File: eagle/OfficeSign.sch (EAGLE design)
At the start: 68 parts, among them Q1 16MHZ, SW3 KMR2, SW4 KMR2, U1 ATMEGA328, U2 L7805CDT-TR, U3 NCS36000, U4 PIR, U5 WS2801, U6 SPX3819, U8 TXB0108PWR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

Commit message: Move Files Around
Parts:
- removed U$10: FIDUCIAL, adafruit:FIDUCIAL
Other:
- moved on the sheet: C16, C17, U8

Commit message: WIP
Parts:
- removed D11: MBR120, microbuilder:DIODE-SCHOTTKYSOD-123
- added D2: MBR120, microbuilder:DIODE-SCHOTTKYSOD-123
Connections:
- net STROBE renamed D2
- removed net D5: U1.PD5(T1)
- removed net D6: U1.PD6(AIN0)
- removed net GPIO4: X2.GPIO5
- removed net GPIO5: X2.GPIO4
- removed net N$17: C15.1, D10.C, D11.C, R21.1, U6.IN
- removed net RST7: U1.PD3(INT1)
- removed net VBAT: D11.A
- new net N$23: C15.1, D10.C, D2.C, R21.1, U6.IN
- new net OCC: U1.PD5(T1), U8.B5
- new net OCC_ESP: U8.A5, X2.GPIO5
- new net RES: U1.PD6(AIN0), U8.B6
- new net RES_ESP: U8.A6, X2.GPIO4
- net OUT: now also U1.PD3(INT1)
- net VCC: now also D2.A
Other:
- moved on the sheet: C14, C15, C16, C17, D10, D12, D8, D9, JP6, R18, R19, R20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

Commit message: Moves and Shakes
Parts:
- added POT: (no value), SparkFun-Connectors:M04JST-PTH
- added R15: 3.3, adafruit:R-US_M0805
- added U7: NJVMJD2955T4G, bg_eagle_lib:NJVMJD2955T4G
- C19: value 10uF -> 0.33uF
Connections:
- new net N$24: POT.3
- new net N$25: POT.2
- new net N$26: JP4.PWR, R15.2, U7.E
- net GND: now also POT.1
- net RAW: now also R15.1, U7.B; no longer JP4.PWR
- net VCC: now also POT.4, U7.C
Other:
- moved on the sheet: C10, C19, JP4, LED1, R11, U2

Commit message: Add Indicator
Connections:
- removed net A1: U1.PC1(ADC1)
- removed net N$24: POT.3
- new net POT: POT.3, U1.PC1(ADC1)
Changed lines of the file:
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@@
 <?xml version="1.0" encoding="utf-8"?>
 <!DOCTYPE eagle SYSTEM "eagle.dtd">
-<eagle version="8.7.0">
+<eagle version="8.7.1">
 <drawing>
 <settings>
@@
 </segment>
 </net>
-<net name="A1" class="0">
+<net name="POT" class="0">
 <segment>
 <wire x1="231.14" y1="160.02" x2="233.68" y2="160.02" width="0.1524" layer="91"/>
 <pinref part="U1" gate="G$1" pin="PC1(ADC1)"/>
 <label x="233.68" y="160.02" size="1.27" layer="95" xref="yes"/>
+</segment>
+<segment>
+<pinref part="POT" gate="G$1" pin="3"/>
+<wire x1="25.4" y1="254" x2="27.94" y2="254" width="0.1524" layer="91"/>
+<label x="27.94" y="254" size="1.27" layer="95" xref="yes"/>
 </segment>
 </net>
@@
 </segment>
 </net>
-<net name="N$24" class="0">
-<segment>
-<pinref part="POT" gate="G$1" pin="3"/>
-<wire x1="25.4" y1="254" x2="27.94" y2="254" width="0.1524" layer="91"/>
-</segment>
-</net>

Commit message: wip
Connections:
- net D2 renamed POD_IND
- net N$25 renamed POT_IND
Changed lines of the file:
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@@
 </segment>
 </net>
-<net name="D2" class="0">
+<net name="POD_IND" class="0">
 <segment>
 <wire x1="231.14" y1="134.62" x2="233.68" y2="134.62" width="0.1524" layer="91"/>
@@
 </segment>
 </net>
-<net name="N$25" class="0">
+<net name="POT_IND" class="0">
 <segment>
 <pinref part="POT" gate="G$1" pin="2"/>
 <wire x1="27.94" y1="251.46" x2="25.4" y2="251.46" width="0.1524" layer="91"/>
-</segment>
-</net>
+<label x="27.94" y="251.46" size="1.27" layer="95" xref="yes"/>
+</segment>
+</net>

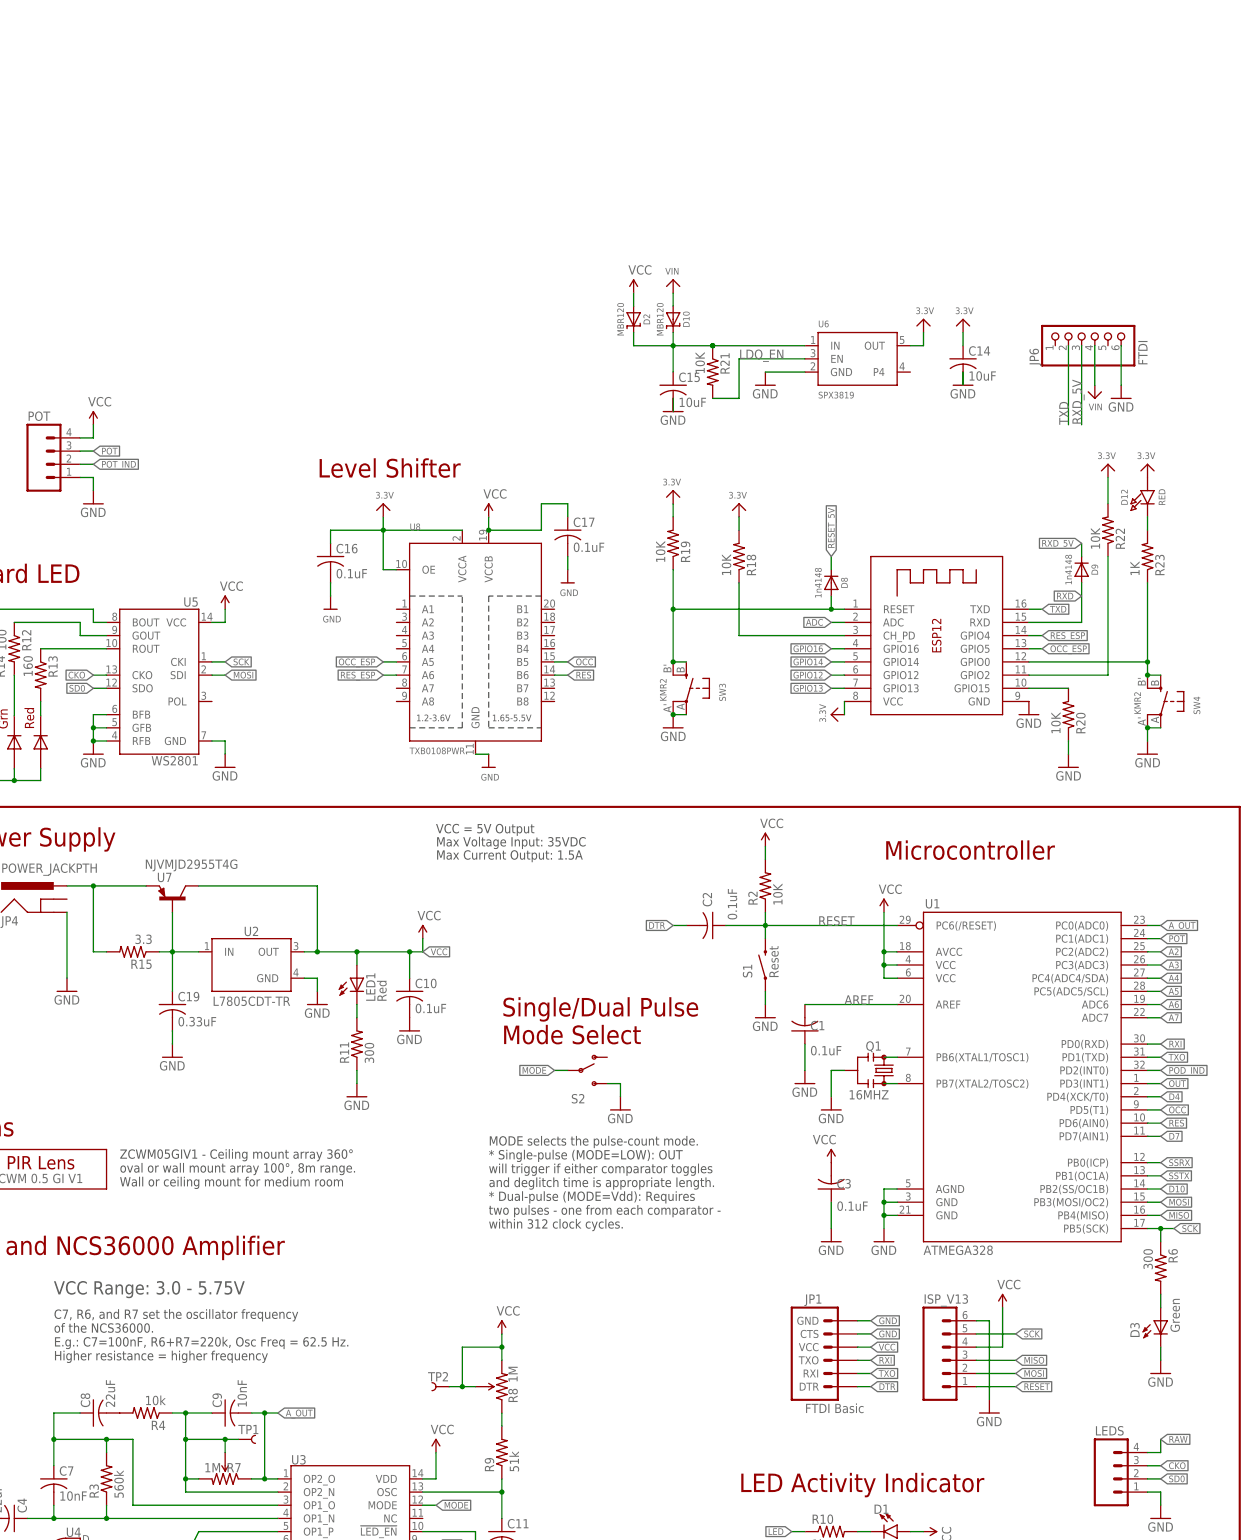
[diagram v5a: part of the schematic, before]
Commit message: Add Remote Motion / Work on Dispaly
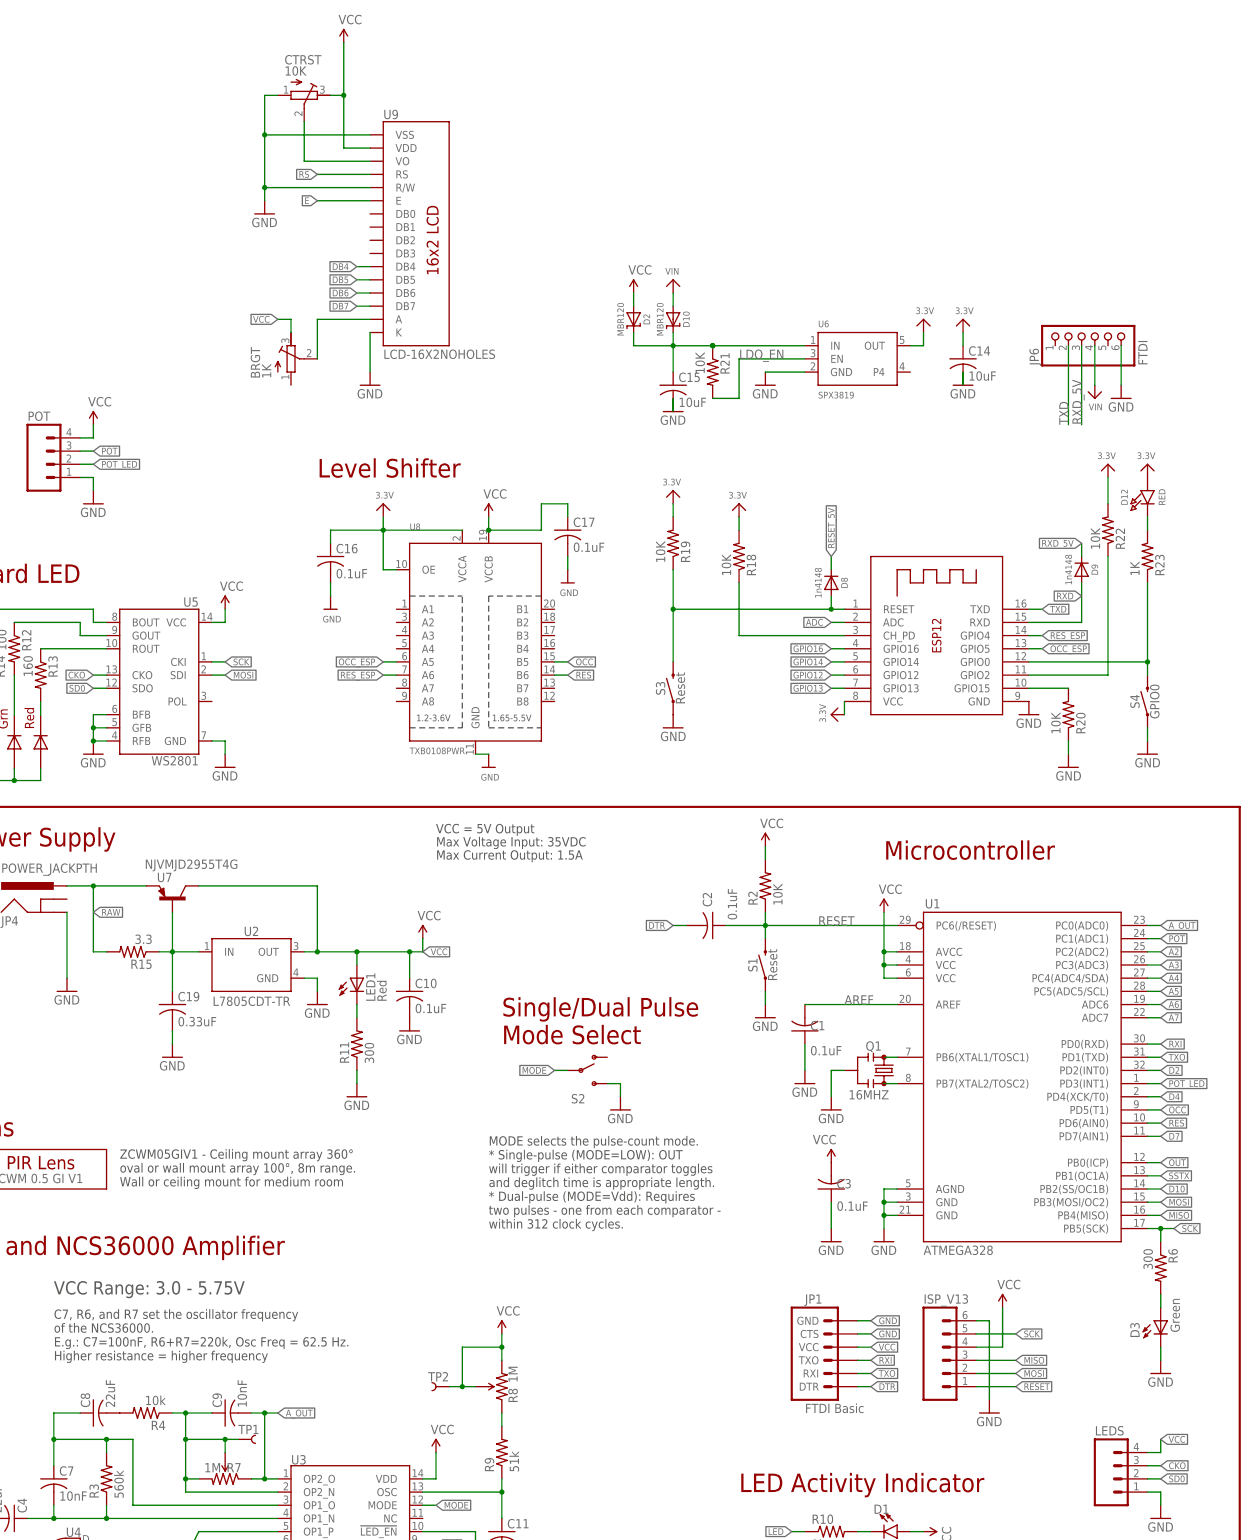
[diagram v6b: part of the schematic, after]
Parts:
- removed SW3, SW4: KMR2, microbuilder:SWITCH_TACT_SMT4.6X2.8
- added BRGT: 1K, resistor:R-TRIMM3296W
- added CTRST: 10K, resistor:R-TRIMM3296W
- added S3: Reset, SparkFun-Switches:MOMENTARY-SWITCH-SPST-SMD-5.2-REDUNDANT
- added S4: GPIO0, SparkFun-Switches:MOMENTARY-SWITCH-SPST-SMD-5.2-REDUNDANT
- added U9: LCD-16X2NOHOLES, SparkFun-Displays:LCD-16X2NOHOLES
- S1: device Testing:SWITCH-MOMENTARY-2SMD-ALT01 -> SparkFun-Switches:MOMENTARY-SWITCH-SPST-SMD-5.2-REDUNDANT
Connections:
- net POD_IND renamed D2
- removed net N$26: JP4.PWR, R15.2, U7.E
- removed net POT_IND: POT.2
- removed net SSRX: U1.PB0(ICP)
- new net A1: BRGT.S, U9.A
- new net DB4: U9.DB4
- new net DB5: U9.DB5
- new net DB6: U9.DB6
- new net DB7: U9.DB7
- new net E: U9.E
- new net L7805_IN: C19.1, R15.1, U2.IN, U7.B
- new net POT_LED: POT.2, U1.PD3(INT1)
- new net RS: U9.RS
- new net VO: CTRST.S, U9.VO
- net GND: now also CTRST.A, S3.1, S4.1, U9.K, U9.R/W, U9.VSS; no longer SW3.P, SW3.P1, SW4.P, SW4.P1
- net GPIO0: now also S4.2; no longer SW4.S, SW4.S1
- net OUT: now also U1.PB0(ICP); no longer U1.PD3(INT1)
- net RAW: now also JP4.PWR, R15.2, U7.E; no longer C19.1, LEDS.4, R15.1, U2.IN, U7.B
- net RESET_HZA: now also S3.2; no longer SW3.S, SW3.S1
- net VCC: now also BRGT.E, CTRST.E, LEDS.4, U9.VDD

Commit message: Add Display / Add Indicator LEDs
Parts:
- removed D12: RED, microbuilder:LED0805_NOOUTLINE
- added D4: Green, led:LEDCHIPLED_0805
- added D5: Red, led:LEDCHIPLED_0805
- added LED3: RED, led:LEDCHIP-LED0805
- added R16: 1k, adafruit:R-US_M0805
- added R17: 300, adafruit:R-US_M0805
- D1: device SparkFun-LED:LED-GREEN1206-BOTTOM -> led:LEDCHIPLED_0805
- D3, LED1: device adafruit:LEDCHIPLED_0805 -> led:LEDCHIPLED_0805
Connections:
- removed net DB4: U9.DB4
- removed net DB5: U9.DB5
- removed net DB6: U9.DB6
- removed net DB7: U9.DB7
- removed net GPIO12: X2.GPIO12
- removed net GPIO13: X2.GPIO13
- removed net GPIO14: X2.GPIO14
- removed net GPIO15: R20.2, X2.GPIO15
- removed net GPIO16: X2.GPIO16
- removed net GPIO2: R22.1, X2.GPIO2
- removed net RS: U9.RS
- new net E_ESP: R22.1, U8.A2, X2.GPIO2
- new net LCD4_ESP: U8.A3, X2.GPIO16
- new net LCD5_ESP: U8.A4, X2.GPIO14
- new net LCD6_ESP: U8.A5, X2.GPIO12
- new net LCD7_ESP: U8.A6, X2.GPIO13
- new net LCD_D4: U8.B3, U9.DB4
- new net LCD_D5: U8.B4, U9.DB5
- new net LCD_D6: U8.B5, U9.DB6
- new net LCD_D7: U8.B6, U9.DB7
- new net LCD_E: U9.E
- new net LCD_RS: U8.B1, U9.RS
- new net N$17: LED3.C, R23.2
- new net N$24: D4.C, R16.2
- new net RS_ESP: R20.2, U8.A1, X2.GPIO15
- net 3.3V: now also LED3.A; no longer D12.A
- net E: now also U8.B2; no longer U9.E
- net GND: now also R16.1, R17.1
- net N$18: now also D5.C, R17.2; no longer D12.C, R23.2
- net OCC: now also D4.A, U8.B7; no longer U8.B5
- net OCC_ESP: now also U8.A7; no longer U8.A5
- net RES: now also U8.B8; no longer U8.B6
- net RES_ESP: now also D5.A, U8.A8; no longer U8.A6
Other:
- moved on the sheet: C16, R20, S4

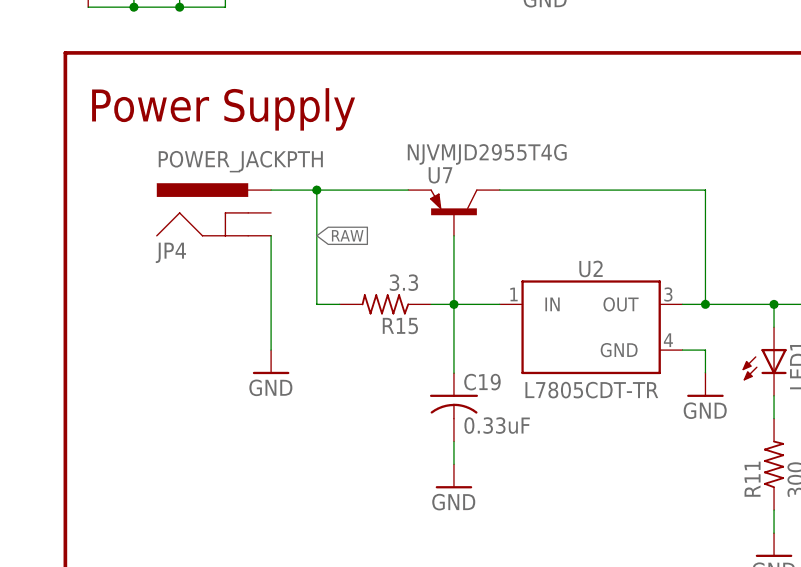
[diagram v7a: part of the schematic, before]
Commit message: Screen is plugged in but doesnt work
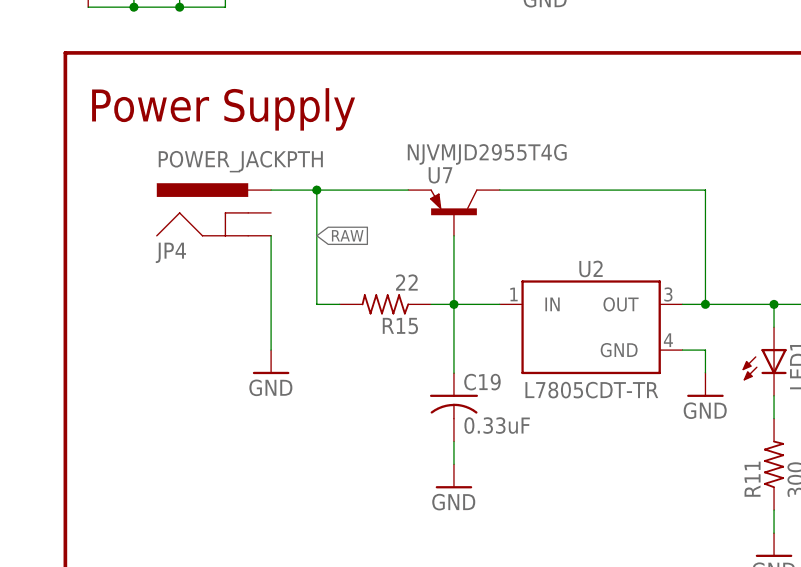
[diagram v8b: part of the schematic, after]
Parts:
- R15: value 3.3 -> 22
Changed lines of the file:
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@@
 <part name="SUPPLY11" library="SparkFun-Aesthetics" deviceset="VCC" device=""/>
 <part name="U7" library="bg_eagle_lib" deviceset="NJVMJD2955T4G" device=""/>
-<part name="R15" library="adafruit" deviceset="R-US_" device="M0805" value="3.3"/>
+<part name="R15" library="adafruit" deviceset="R-US_" device="M0805" value="22"/>
 <part name="GND22" library="SparkFun" deviceset="GND" device=""/>
 <part name="S3" library="SparkFun-Switches" deviceset="MOMENTARY-SWITCH-SPST" device="-SMD-5.2-REDUNDANT" value="Reset"/>
